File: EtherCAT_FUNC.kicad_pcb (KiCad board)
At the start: 2 copper layers, 33.7 x 46.7 mm, 51 parts, among them J1 axt430124, J2 Conn_01x02, J3 Conn_01x02, J4 Conn_01x04, J5 Conn_01x02, J6 Conn_01x04, J7 Conn_01x04, J8 Conn_01x03, J9 Conn_01x08, U1 SY8303AAIC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

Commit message: Change conns of GPIO
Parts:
- added J10: Conn_01x02, Connector_JST:JST_GH_BM02B-GHS-TBT_1x02-1MP_P1.25mm_Vertical, F.Cu at (146.0, 121.8)
- added J11: Conn_01x02, Connector_JST:JST_GH_BM02B-GHS-TBT_1x02-1MP_P1.25mm_Vertical, F.Cu at (150.1, 129.4)
- added J12: Conn_01x02, Connector_JST:JST_GH_BM02B-GHS-TBT_1x02-1MP_P1.25mm_Vertical, F.Cu at (154.0, 114.3)
- added J13: Conn_01x02, Connector_JST:JST_GH_BM02B-GHS-TBT_1x02-1MP_P1.25mm_Vertical, F.Cu at (154.0, 121.8)
- added J14: Conn_01x02, Connector_JST:JST_GH_BM02B-GHS-TBT_1x02-1MP_P1.25mm_Vertical, F.Cu at (158.1, 129.4)
- added J15: Conn_01x02, Connector_JST:JST_GH_BM02B-GHS-TBT_1x02-1MP_P1.25mm_Vertical, F.Cu at (162.0, 114.3)
- added J16: Conn_01x02, Connector_JST:JST_GH_BM02B-GHS-TBT_1x02-1MP_P1.25mm_Vertical, F.Cu at (162.0, 121.8)
- H4, H5, H6, H7: footprint MountingHole:MountingHole_2.7mm_M2.5 -> EXTRA IC:M1.6
- J9: value Conn_01x08 -> Conn_01x02; footprint Connector_PinHeader_2.54mm:PinHeader_1x08_P2.54mm_Vertical -> Connector_JST:JST_GH_BM02B-GHS-TBT_1x02-1MP_P1.25mm_Vertical
- moved H4 16.4 mm to (168.8, 130.4)
- moved H5 16.4 mm to (139.2, 130.4)
- moved H6 1.13 mm to (139.2, 72.2)
- moved H7 1.13 mm to (168.8, 72.2)
- moved J9 1.01 mm to (146.0, 114.3), turned to 180 degrees
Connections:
- J9 pad 1: /GPIO1 -> GND
- J9 pad 2: /GPIO2 -> /GPIO1
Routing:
- net /GPIO6: track 23.3 -> 35.8 mm
- net /GPIO3: track 30.2 -> 39.4 mm
- net /GPIO1: track 31.2 -> 25.5 mm
- net /GPIO5: track 22.5 -> 27.7 mm
- net /GPIO8: track 25.1 -> 30.2 mm
- net /GPIO2: track 29.4 -> 33.2 mm
- net /GPIO4: track 22.8 -> 20.0 mm
- net /GPIO7: track 24.2 -> 22.2 mm
- net LED_CAN1: track 33.4 -> 35.3 mm
- net GND: vias 14 -> 17
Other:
- board size 33.7 x 46.7 mm -> 33.7 x 62.4 mm

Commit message: Change footprints of M2 and axt330124
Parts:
- J1: footprint EXTRA IC:axt430124 -> EXTRA IC:axt330124
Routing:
- net /GPIO3: track 39.4 -> 40.4 mm
- net /GPIO2: track 33.2 -> 34.0 mm
- net /GPIO1: track 25.5 -> 26.3 mm
- net +5V: track 73.6 -> 72.9 mm, vias 5 -> 4
- net LED_CAN0: track 21.6 -> 22.2 mm
- net /SPI_SCS: track 17.7 -> 18.3 mm
- net /SPI_SCK: track 16.4 -> 17.0 mm
- net /SPI_MOSI: track 15.2 -> 15.8 mm
- net /SPI_MISO: track 14.0 -> 14.6 mm
- net /UART_TX: track 20.2 -> 19.6 mm
- net /UART_RX: track 17.9 -> 17.3 mm
- net /GPIO8: track 30.2 -> 29.6 mm
- net /GPIO7: track 22.2 -> 21.6 mm
- net /GPIO6: track 35.8 -> 35.2 mm
- net /GPIO5: track 27.7 -> 27.1 mm
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
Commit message: All 0603 version
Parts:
- C2, C3, C5, C6, C7, C8: footprint Capacitor_SMD:C_0402_1005Metric -> Capacitor_SMD:C_0603_1608Metric
- D1, D2, D3, D4, D5: footprint LED_SMD:LED_0402_1005Metric -> LED_SMD:LED_0603_1608Metric
- R1, R2, R3, R4, R5, R6, R7: footprint Resistor_SMD:R_0402_1005Metric -> Resistor_SMD:R_0603_1608Metric
- R10, R8, R9: footprint Resistor_SMD:R_0402_1005Metric -> Resistor_SMD:R_0603_1608Metric; moved to B.Cu
- moved C4 2.53 mm to (158.8, 73.0)
- moved R2 2.38 mm to (157.0, 73.2)
- moved C3 1.94 mm to (155.5, 73.2)
- moved R3 1.90 mm to (156.3, 71.0), turned to 0 degrees
- moved R4 1.36 mm to (166.3, 93.9)
- moved R5 1.35 mm to (166.3, 110.5)
- moved C8 0.70 mm to (150.9, 99.6)
- moved C7 0.70 mm to (150.9, 105.1)
- moved D5 0.62 mm to (167.7, 86.5)
- moved D3 0.58 mm to (167.7, 89.4)
- moved C6 0.55 mm to (160.6, 97.0), turned to 0 degrees
- moved C5 0.55 mm to (160.5, 102.5), turned to 0 degrees
- moved R10 0.48 mm to (166.1, 86.5)
- moved R1 0.47 mm to (154.1, 71.7)
- moved R8 0.46 mm to (166.1, 89.4)
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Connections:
- J10 pad 1: GND -> /GPIO2
- J10 pad 2: /GPIO2 -> GND
- J11 pad 1: GND -> /GPIO3
- J11 pad 2: /GPIO3 -> GND
- J12 pad 1: GND -> /GPIO4
- J12 pad 2: /GPIO4 -> GND
- J13 pad 1: GND -> /GPIO5
- J13 pad 2: /GPIO5 -> GND
- J14 pad 1: GND -> /GPIO6
- J14 pad 2: /GPIO6 -> GND
- J15 pad 1: GND -> /GPIO7
- J15 pad 2: /GPIO7 -> GND
- J16 pad 1: GND -> /GPIO8
- J16 pad 2: /GPIO8 -> GND
- J9 pad 1: GND -> /GPIO1
- J9 pad 2: /GPIO1 -> GND
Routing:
- net +5V: track 72.9 -> 67.3 mm, vias 4 -> 3
- net Net-(U1-FB): track 3.07 -> 6.38 mm
- net +24V: track 36.0 -> 37.5 mm, vias 2 -> 1
- net 3V3: track 56.0 -> 54.8 mm, vias 3 -> 4
- net LED_CAN1: track 35.3 -> 36.5 mm
- net /CAN/FDCAN2_RX: track 11.0 -> 12.2 mm
- net /CAN/FDCAN2_TX: track 16.0 -> 14.8 mm
- net Net-(D3-A): track 0.93 -> 2.12 mm, vias 0 -> 1
- net Net-(D4-A): track 0.93 -> 2.12 mm, vias 0 -> 1
- net Net-(D5-A): track 0.93 -> 2.07 mm, vias 0 -> 1
- net LED_CAN0: track 22.2 -> 21.6 mm
- net /GPIO7: track 21.6 -> 22.1 mm
- net /GPIO6: track 35.2 -> 35.7 mm
- net /GPIO3: track 40.4 -> 41.0 mm
- net /GPIO2: track 34.0 -> 33.5 mm
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
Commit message: Official version
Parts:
- added H10: MountingHole, EXTRA IC:M1.6, F.Cu at (162.7, 109.1)
- C5, C6, C7, C8, R10, R6, R7, R8, R9, U2, U3, U4, U5, U6: moved to F.Cu
- H4, H5, H6, H7: footprint EXTRA IC:M1.6 -> EXTRA IC:M2_HOLE
- H8, H9: footprint EXTRA IC:M2 -> EXTRA IC:M2_noHOLE
- moved C6 4.50 mm to (160.4, 101.5)
- moved C5 4.46 mm to (160.4, 107.0)
- moved C8 1.47 mm to (150.7, 101.0)
- moved R8 1.44 mm to (166.1, 90.8)
- moved C7 1.43 mm to (150.7, 106.5)
- moved R10 1.35 mm to (164.7, 86.5)
- moved R9 1.35 mm to (164.8, 87.9)
- moved R7 0.44 mm to (159.7, 104.5), turned to -90 degrees
- moved U5 0.43 mm to (162.5, 104.5)
- moved U4 0.39 mm to (162.5, 99.1)
- moved R6 0.38 mm to (159.7, 99.1), turned to -90 degrees
- moved U2 0.33 mm to (155.1, 99.6)
- moved U3 0.31 mm to (155.1, 105.0)
- moved H6 0.13 mm to (139.3, 72.3)
- moved H7 0.13 mm to (168.7, 72.3)
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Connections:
- J1 pad 22: 3V3 -> LED_CAN0
- J1 pad 23: LED_CAN0 -> GND
- J10 pad 1: /GPIO2 -> GND
- J10 pad 2: GND -> /GPIO2
- J11 pad 1: /GPIO3 -> GND
- J11 pad 2: GND -> /GPIO3
- J12 pad 1: /GPIO4 -> GND
- J12 pad 2: GND -> /GPIO4
- J13 pad 1: /GPIO5 -> GND
- J13 pad 2: GND -> /GPIO5
- J14 pad 1: /GPIO6 -> GND
- J14 pad 2: GND -> /GPIO6
- J15 pad 1: /GPIO7 -> GND
- J15 pad 2: GND -> /GPIO7
- J16 pad 1: /GPIO8 -> GND
- J16 pad 2: GND -> /GPIO8
- J9 pad 1: /GPIO1 -> GND
- J9 pad 2: GND -> /GPIO1
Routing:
- net 3V3: track 54.8 -> 59.6 mm
- net /CAN/FDCAN1_TX: track 9.17 -> 4.45 mm, vias 1 -> 0
- net /CAN/FDCAN1_RX: track 4.91 -> 9.47 mm, vias 1 -> 0
- net /CAN/FDCAN2_TX: track 14.8 -> 11.0 mm, vias 1 -> 2
- net /CAN/CAN0_H: track 12.3 -> 9.13 mm, vias 1 -> 0
- net /UART_RX: track 17.5 -> 20.6 mm
- net /CAN/CAN1_L: track 12.3 -> 9.30 mm, vias 1 -> 0
- net /CAN/FDCAN2_RX: track 12.2 -> 15.1 mm, vias 1 -> 2
- net /UART_TX: track 19.9 -> 22.2 mm
- net /CAN/CAN1_H: track 8.42 -> 10.3 mm, vias 1 -> 0
- net +24V: track 37.5 -> 36.1 mm
- net /GPIO8: track 29.9 -> 30.7 mm
- net /CAN/CAN0_L: track 8.42 -> 9.24 mm, vias 1 -> 0
- net Net-(D4-A): track 2.12 -> 1.35 mm, vias 1 -> 0
- net Net-(D5-A): track 2.07 -> 1.36 mm, vias 1 -> 0
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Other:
- outline, holes or cut-outs redrawn

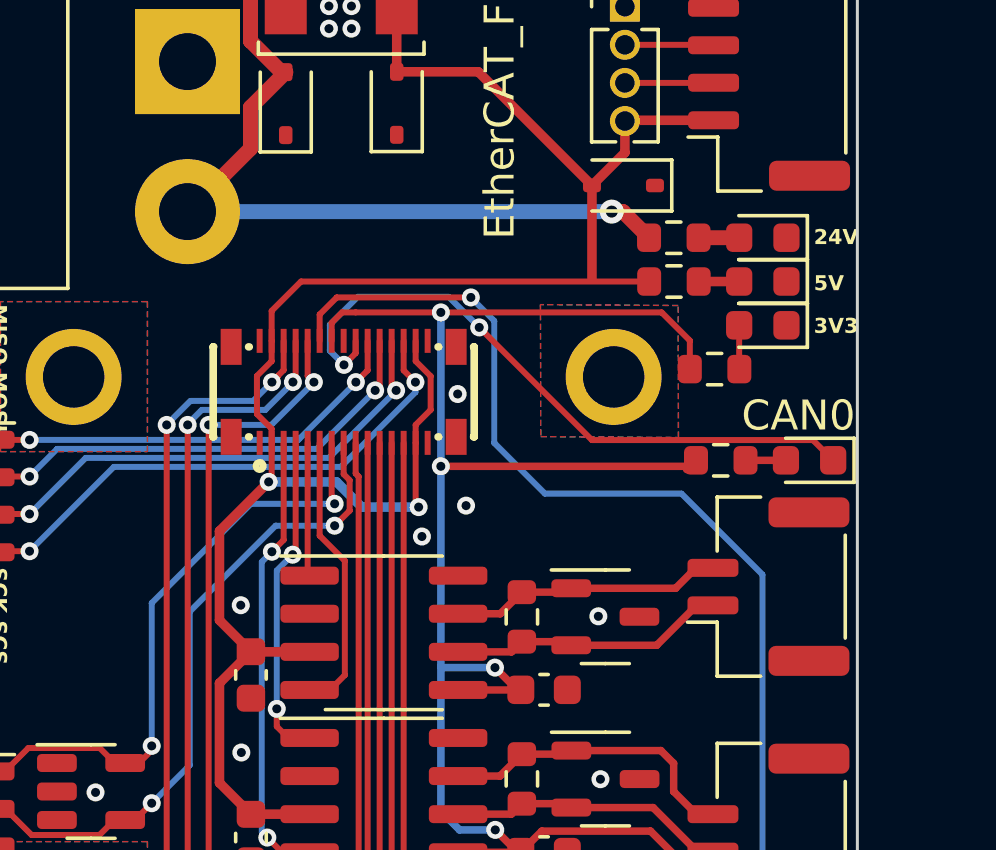
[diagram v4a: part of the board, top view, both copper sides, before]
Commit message: Fixed layout_GND bug
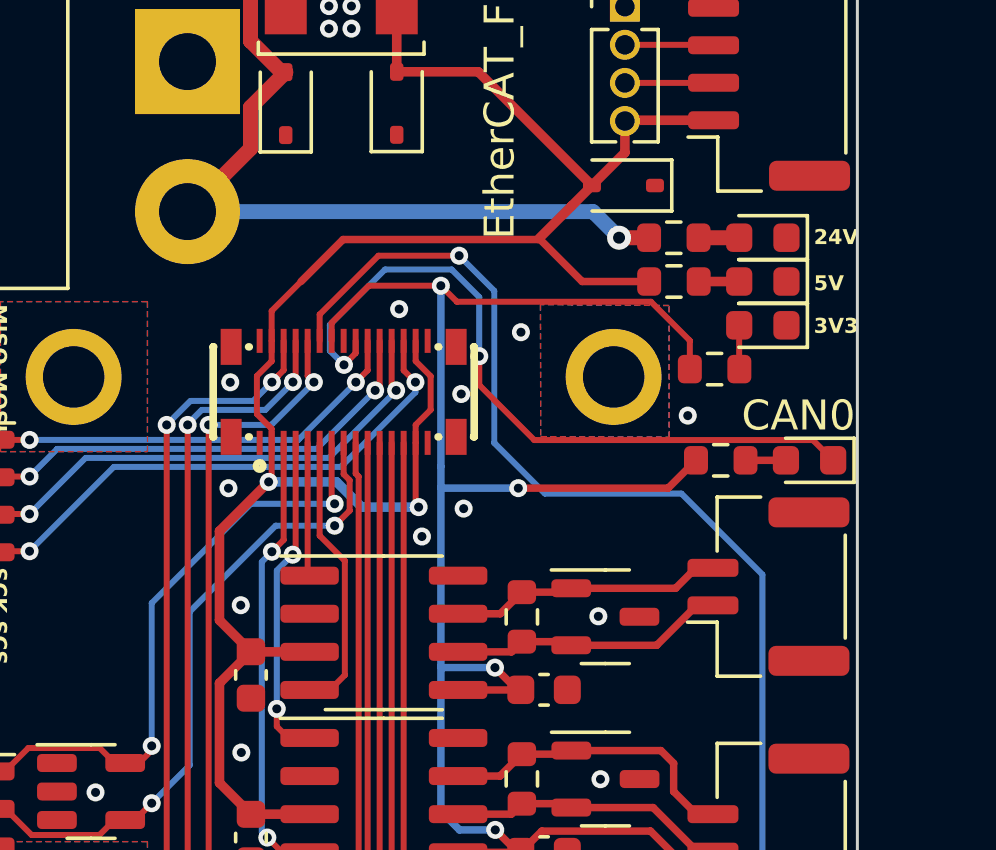
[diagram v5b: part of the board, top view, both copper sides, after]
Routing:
- net LED_CAN0: track 21.9 -> 24.4 mm
- net LED_CAN1: track 36.5 -> 38.2 mm
- net 3V3: track 59.6 -> 61.1 mm
- net +5V: track 67.4 -> 68.0 mm
- net GND: vias 22 -> 27
